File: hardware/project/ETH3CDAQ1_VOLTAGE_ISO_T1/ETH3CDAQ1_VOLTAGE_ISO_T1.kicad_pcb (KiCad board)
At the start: 4 copper layers, 80 x 30 mm, 80 parts, among them J101 GMSTB2,5/2-GF-7,62, J102 Conn_02x10_Odd_Even, U101 DG211, U102 DG419xY, U103 LT3032, U104 OPA140, U105 ISO124, U106 ADuM5410, U107 DCP020515DU, U108 OPA237_SOT23, U109 LT3032-15, U110 74LVC1GU04DRL, U111 74LVC1GU04DRL, U112 74LVC1GU04DRL, U113 24LC08B-E/MS, U114 TXB0104PW, U115 PCA9557PW

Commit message: Voltage module done.
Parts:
- added R25: 10k, Resistor_SMD:R_0603_1608Metric_Pad0.98x0.95mm_HandSolder, B.Cu at (139.8, 54.0)
- added R26: 0, Resistor_SMD:R_0603_1608Metric_Pad0.98x0.95mm_HandSolder, B.Cu at (133.9, 58.5)
- C23: renamed from C115; moved to B.Cu
- U11: renamed from U111; moved to B.Cu
- U12: renamed from U112; moved to F.Cu
- moved C21 4.44 mm to (135.1, 63.9), turned to 180 degrees
- moved C20 3.81 mm to (135.6, 70.1), turned to 180 degrees
- moved C10 3.23 mm to (112.9, 61.1)
- moved R16 3.02 mm to (112.9, 63.5), turned to 0 degrees
- moved U10 2.44 mm to (133.6, 58.2)
- moved U11 2.44 mm to (133.6, 55.9)
- moved U12 2.44 mm to (133.6, 55.9)
- moved C11 2.37 mm to (112.9, 68.6), turned to 0 degrees
- moved R15 2.30 mm to (112.0, 66.0)
- moved R22 2.03 mm to (138.8, 47.0)
- moved R23 1.65 mm to (140.6, 47.0)
- moved SYM1 1.61 mm to (103.8, 56.9)
- moved C6 1.53 mm to (113.8, 57.5)
- moved C7 1.53 mm to (113.8, 49.0)
- moved C8 1.53 mm to (111.3, 49.0)
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- renumbered C101 to C1, C127 to C10, C128 to C11, C106 to C12, C107 to C13, C129 to C14, C130 to C15, C108 to C16, C109 to C17, C110 to C18, C111 to C19, C102 to C2, C112 to C20, C113 to C21, C114 to C22, C116 to C24, C117 to C25, C118 to C26, C119 to C27, C120 to C28, C121 to C29, C103 to C3, C122 to C30, C104 to C4, C105 to C5, C123 to C6, C124 to C7, C125 to C8, C126 to C9, E101 to E1, FB101 to FB1, FB102 to FB2, FB103 to FB3, H101 to H1, H102 to H2, J101 to J1, J102 to J2, L101 to L1, R101 to R1, R110 to R10, R111 to R11, R112 to R12, R113 to R13, R114 to R14, R115 to R15, R116 to R16, R117 to R17, R118 to R18, R119 to R19, R102 to R2, R120 to R20, R121 to R21, R122 to R22, R123 to R23, R124 to R24, R103 to R3, R104 to R4, R105 to R5, R106 to R6, R107 to R7, R108 to R8, R109 to R9, RV101 to RV1, SYM101 to SYM1, U101 to U1, U110 to U10, U113 to U13, U114 to U14, U115 to U15, U102 to U2, U103 to U3, U104 to U4, U105 to U5, U106 to U6, U107 to U7, U108 to U8, U109 to U9
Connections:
- U14 pad 2: Net-(U114-Pad2) -> /IO5
- U14 pad 3: Net-(U114-Pad3) -> /IO4
- U14 pad 4: Net-(U114-Pad4) -> /IO3
- U14 pad 5: Net-(U114-Pad5) -> /IO2
- U14 pad 8: (no net) -> Net-(R25-Pad2)
- U15 pad 10: Net-(U114-Pad3) -> /IO3
- U15 pad 11: Net-(U114-Pad4) -> /IO4
- U15 pad 12: Net-(U114-Pad5) -> /IO5
- U15 pad 9: Net-(U114-Pad2) -> /IO2
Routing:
- net AGNDF: track 0.00 -> 96.2 mm, vias 0 -> 27
- net (no net): track 0.00 -> 71.1 mm
- net +5VF: track 0.00 -> 48.8 mm, vias 0 -> 6
- net -15VF: track 0.00 -> 39.8 mm, vias 0 -> 10
- net +15VF: track 0.00 -> 28.1 mm, vias 0 -> 7
- net /SCL: track 0.00 -> 25.2 mm, vias 0 -> 1
- net Net-(R15-Pad1): track 0.00 -> 22.7 mm, vias 0 -> 2
- net /AOUT: track 0.00 -> 22.7 mm
- net /G1: track 0.00 -> 21.8 mm
- net /G10: track 0.00 -> 20.0 mm, vias 0 -> 2
- net Net-(U1-Pad11): track 0.00 -> 18.6 mm
- net Net-(R20-Pad2): track 0.00 -> 18.4 mm, vias 0 -> 1
- net /A0: track 0.00 -> 18.0 mm, vias 0 -> 1
- net /SDA: track 0.00 -> 17.9 mm, vias 0 -> 1
- net Net-(C1-Pad1): track 0.00 -> 16.4 mm
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- added copper zone on B.Cu, net +15V
- added copper zone on F.Cu, net +15V
- added copper zone on In2.Cu, net +15V
- added copper zone on B.Cu, net +15VF
- added copper zone on F.Cu, net +15VF
- added copper zone on In2.Cu, net +15VF
- added copper zone on In2.Cu, net +18V
- added copper zone on In2.Cu, net +3V3
- added copper zone on B.Cu, net +5V
- added copper zone on F.Cu, net +5V
- added copper zone on In2.Cu, net +5V
- added copper zone on B.Cu, net -15V
- added copper zone on F.Cu, net -15V
- added copper zone on In2.Cu, net -15V
- added copper zone on B.Cu, net -15VF
- added copper zone on F.Cu, net -15VF
- added copper zone on In2.Cu, net -15VF
- added copper zone on In2.Cu, net -18V
- added copper zone on F.Cu, net AGNDF
- added copper zone on In1.Cu, net AGNDF
- added copper zone on B.Cu, net GND
- added copper zone on F.Cu, net GND
- added copper zone on In1.Cu, net GND
- added copper zone on B.Cu, net VCC
- added copper zone on F.Cu, net VCC
- added copper zone on In2.Cu, net VCC
- added copper zone on B.Cu, net VDD
- added copper zone on F.Cu, net VDD
- added copper zone on In2.Cu, net VDD
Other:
- outline, holes or cut-outs redrawn
- net class Default: clearance 0.2 -> 0.127; trace_width 0.25 -> 0.127; via_dia 0.8 -> 0.5; via_drill 0.4 -> 0.2
- rule trace_clearance: 0.2 -> 0.127
- rule trace_min: 0.2 -> 0.12
- rule via_min_drill: 0.3 -> 0.2
- board text added: "1"
- board text added: "2"
- board text added: "3"
- board text added: "4"
- board text added: "ONLY PLASTIC SPACER"

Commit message: Modifications in PCBs.
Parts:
- moved C30 0.65 mm to (140.6, 50.8)
- moved R24 0.65 mm to (138.8, 50.8)

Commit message: PCB design
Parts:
- added C31: 10u, Capacitor_SMD:C_0603_1608Metric_Pad1.08x0.95mm_HandSolder, B.Cu at (134.0, 48.5)
- added C32: 100n, Capacitor_SMD:C_0603_1608Metric_Pad1.08x0.95mm_HandSolder, B.Cu at (134.0, 46.1)
- C14, C15: value 100n -> 10u
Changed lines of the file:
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@@
-(kicad_pcb (version 20171130) (host pcbnew "(5.1.8)-1")
+(kicad_pcb (version 20171130) (host pcbnew 5.1.8)
   (general
     (thickness 1.6)
@@
     (tracks 778)
     (zones 0)
-    (modules 82)
+    (modules 84)
     (nets 65)
   )
@@
   )
   (setup
-    (last_trace_width 0.381)
+    (last_trace_width 0.127)
     (user_trace_width 0.254)
     (user_trace_width 0.381)
@@
     (add_net "Net-(C5-Pad2)")
     (add_net "Net-(E1-Pad1)")
+    (add_net "Net-(J2-Pad17)")
+    (add_net "Net-(J2-Pad5)")
+    (add_net "Net-(J2-Pad6)")
     (add_net "Net-(L1-Pad2)")
     (add_net "Net-(R1-Pad2)")
@@
     (add_net "Net-(U1-Pad11)")
     (add_net "Net-(U1-Pad6)")
+    (add_net "Net-(U10-Pad1)")
+    (add_net "Net-(U11-Pad1)")
     (add_net "Net-(U11-Pad2)")
+    (add_net "Net-(U12-Pad1)")
     (add_net "Net-(U12-Pad2)")
+    (add_net "Net-(U14-Pad6)")
+    (add_net "Net-(U14-Pad9)")
+    (add_net "Net-(U15-Pad13)")
+    (add_net "Net-(U15-Pad14)")
+    (add_net "Net-(U15-Pad6)")
     (add_net "Net-(U2-Pad1)")
+    (add_net "Net-(U3-Pad13)")
+    (add_net "Net-(U4-Pad1)")
+    (add_net "Net-(U4-Pad5)")
+    (add_net "Net-(U4-Pad8)")
+    (add_net "Net-(U6-Pad17)")
+    (add_net "Net-(U6-Pad7)")
+    (add_net "Net-(U6-Pad8)")
+    (add_net "Net-(U9-Pad13)")
+    (add_net "Net-(U9-Pad2)")
+    (add_net "Net-(U9-Pad8)")
     (add_net VCC)
     (add_net VDD)
   )
+  (module Capacitor_SMD:C_0603_1608Metric_Pad1.08x0.95mm_HandSolder (layer B.Cu)
+    (at 133.985 46.101 180)
+    (descr "Capacitor SMD 0603 (1608 Metric), square (rectangular) end terminal, IPC_7351 nominal with elongated pad for handsoldering. (Body size source: IPC-SM-782 page 76, https://www.pcb-3d.com/wordpress/wp-content/uploads/ipc-sm-782a_amendment_1_and_2.pdf), generated with kicad-footprint-generator")
+    (tags "capacitor handsolder")
+    (attr smd)
+    (fp_text reference C32 (at 0 1.113) (layer B.SilkS)
+      (effects (font (size 0.6 0.6) (thickness 0.12)) (justify mirror))
+    )
+    (fp_text value 100n (at 0 -1.43) (layer B.Fab)
+      (effects (font (size 1 1) (thickness 0.15)) (justify mirror))
+    )
+    (fp_line (start 1.65 -0.73) (end -1.65 -0.73) (layer B.CrtYd) (width 0.05))
+    (fp_line (start 1.65 0.73) (end 1.65 -0.73) (layer B.CrtYd) (width 0.05))
+    (fp_line (start -1.65 0.73) (end 1.65 0.73) (layer B.CrtYd) (width 0.05))
+    (fp_line (start -1.65 -0.73) (end -1.65 0.73) (layer B.CrtYd) (width 0.05))
+    (fp_line (start -0.146267 -0.51) (end 0.146267 -0.51) (layer B.SilkS) (width 0.12))
+    (fp_line (start -0.146267 0.51) (end 0.146267 0.51) (layer B.SilkS) (width 0.12))
+    (fp_line (start 0.8 -0.4) (end -0.8 -0.4) (layer B.Fab) (width 0.1))
+    (fp_line (start 0.8 0.4) (end 0.8 -0.4) (layer B.Fab) (width 0.1))
+    (fp_line (start -0.8 0.4) (end 0.8 0.4) (layer B.Fab) (width 0.1))
+    (fp_line (start -0.8 -0.4) (end -0.8 0.4) (layer B.Fab) (width 0.1))
+    (fp_text user %R (at 0 0) (layer B.Fab)
+      (effects (font (size 0.4 0.4) (thickness 0.06)) (justify mirror))
+    )
+    (pad 2 smd roundrect (at 0.8625 0 180) (size 1.075 0.95) (layers B.Cu B.Paste B.Mask) (roundrect_rratio 0.25)
+      (net 6 GND))
+    (pad 1 smd roundrect (at -0.8625 0 180) (size 1.075 0.95) (layers B.Cu B.Paste B.Mask) (roundrect_rratio 0.25)
+      (net 7 +5V))
+    (model ${KISYS3DMOD}/Capacitor_SMD.3dshapes/C_0603_1608Metric.wrl
+      (at (xyz 0 0 0))
+      (scale (xyz 1 1 1))
+      (rotate (xyz 0 0 0))
+    )
+  )
+  (module Capacitor_SMD:C_0603_1608Metric_Pad1.08x0.95mm_HandSolder (layer B.Cu)
+    (at 133.985 48.514 180)
+    (descr "Capacitor SMD 0603 (1608 Metric), square (rectangular) end terminal, IPC_7351 nominal with elongated pad for handsoldering. (Body size source: IPC-SM-782 page 76, https://www.pcb-3d.com/wordpress/wp-content/uploads/ipc-sm-782a_amendment_1_and_2.pdf), generated with kicad-footprint-generator")
+    (tags "capacitor handsolder")
+    (attr smd)
+    (fp_text reference C31 (at 0 1.143) (layer B.SilkS)
+      (effects (font (size 0.6 0.6) (thickness 0.12)) (justify mirror))
+    )
+    (fp_text value 10u (at 0 -1.43) (layer B.Fab)
+      (effects (font (size 1 1) (thickness 0.15)) (justify mirror))
+    )
+    (fp_line (start 1.65 -0.73) (end -1.65 -0.73) (layer B.CrtYd) (width 0.05))
+    (fp_line (start 1.65 0.73) (end 1.65 -0.73) (layer B.CrtYd) (width 0.05))
+    (fp_line (start -1.65 0.73) (end 1.65 0.73) (layer B.CrtYd) (width 0.05))
+    (fp_line (start -1.65 -0.73) (end -1.65 0.73) (layer B.CrtYd) (width 0.05))
+    (fp_line (start -0.146267 -0.51) (end 0.146267 -0.51) (layer B.SilkS) (width 0.12))
+    (fp_line (start -0.146267 0.51) (end 0.146267 0.51) (layer B.SilkS) (width 0.12))
+    (fp_line (start 0.8 -0.4) (end -0.8 -0.4) (layer B.Fab) (width 0.1))
+    (fp_line (start 0.8 0.4) (end 0.8 -0.4) (layer B.Fab) (width 0.1))
+    (fp_line (start -0.8 0.4) (end 0.8 0.4) (layer B.Fab) (width 0.1))
+    (fp_line (start -0.8 -0.4) (end -0.8 0.4) (layer B.Fab) (width 0.1))
+    (fp_text user %R (at 0 0) (layer B.Fab)
+      (effects (font (size 0.4 0.4) (thickness 0.06)) (justify mirror))
+    )
+    (pad 2 smd roundrect (at 0.8625 0 180) (size 1.075 0.95) (layers B.Cu B.Paste B.Mask) (roundrect_rratio 0.25)
+      (net 6 GND))
+    (pad 1 smd roundrect (at -0.8625 0 180) (size 1.075 0.95) (layers B.Cu B.Paste B.Mask) (roundrect_rratio 0.25)
+      (net 7 +5V))
+    (model ${KISYS3DMOD}/Capacitor_SMD.3dshapes/C_0603_1608Metric.wrl
+      (at (xyz 0 0 0))
+      (scale (xyz 1 1 1))
+      (rotate (xyz 0 0 0))
+    )
+  )
   (module ETH3CDAQ1:NLV32 (layer B.Cu)
     (at 83.947 52.959)
@@
       (effects (font (size 0.6 0.6) (thickness 0.12)) (justify mirror))
     )
-    (fp_text value 100n (at 0 -1.43) (layer B.Fab)
+    (fp_text value 10u (at 0 -1.43) (layer B.Fab)
       (effects (font (size 0.6 0.6) (thickness 0.12)) (justify mirror))
     )
@@
       (effects (font (size 0.6 0.6) (thickness 0.12)) (justify mirror))
     )
-    (fp_text value 100n (at 0 -1.43) (layer B.Fab)
+    (fp_text value 10u (at 0 -1.43) (layer B.Fab)
       (effects (font (size 0.6 0.6) (thickness 0.12)) (justify mirror))
     )
@@
     (polygon
       (pts
-        (xy 136.144 44.958) (xy 134.112 44.958) (xy 134.112 42.291) (xy 136.144 42.291)
+        (xy 136.398 49.657) (xy 134.112 49.657) (xy 134.112 42.291) (xy 136.398 42.291)
       )
     )

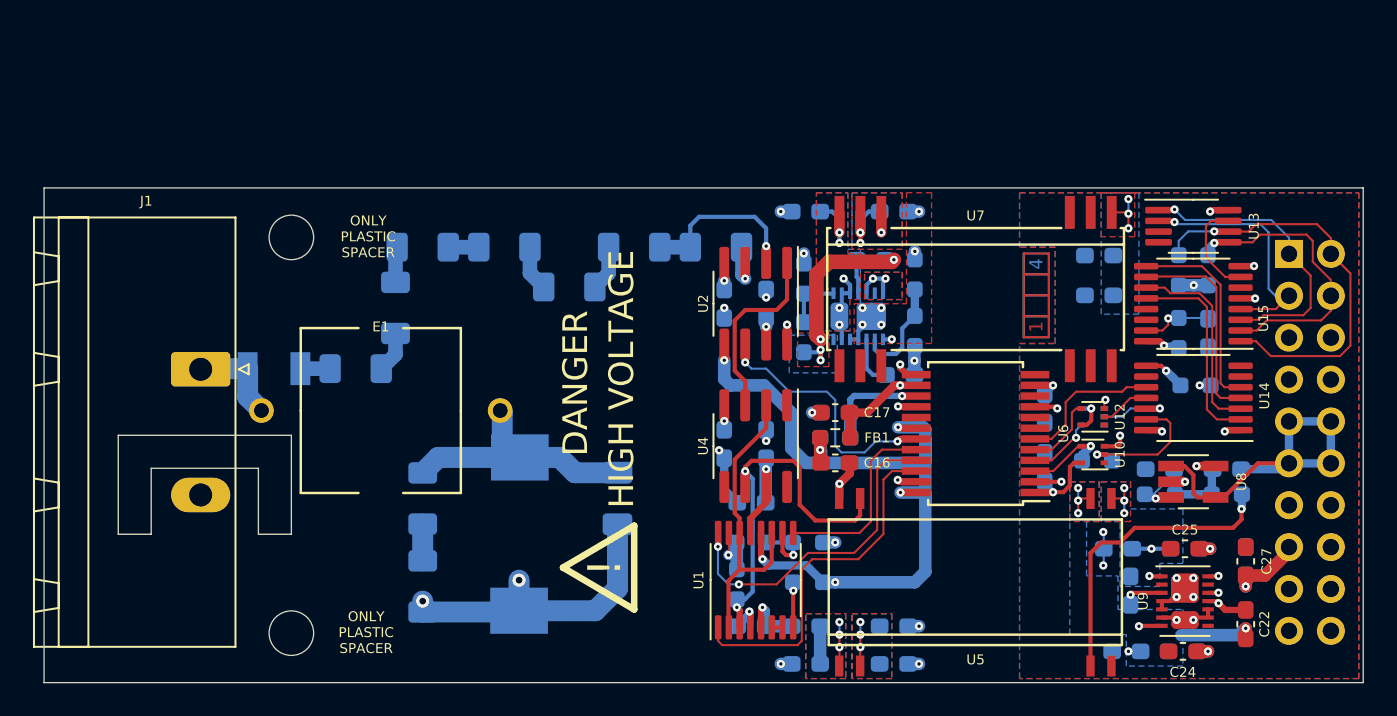
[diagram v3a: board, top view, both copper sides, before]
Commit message: Modification in PCBs. Created BOM files.
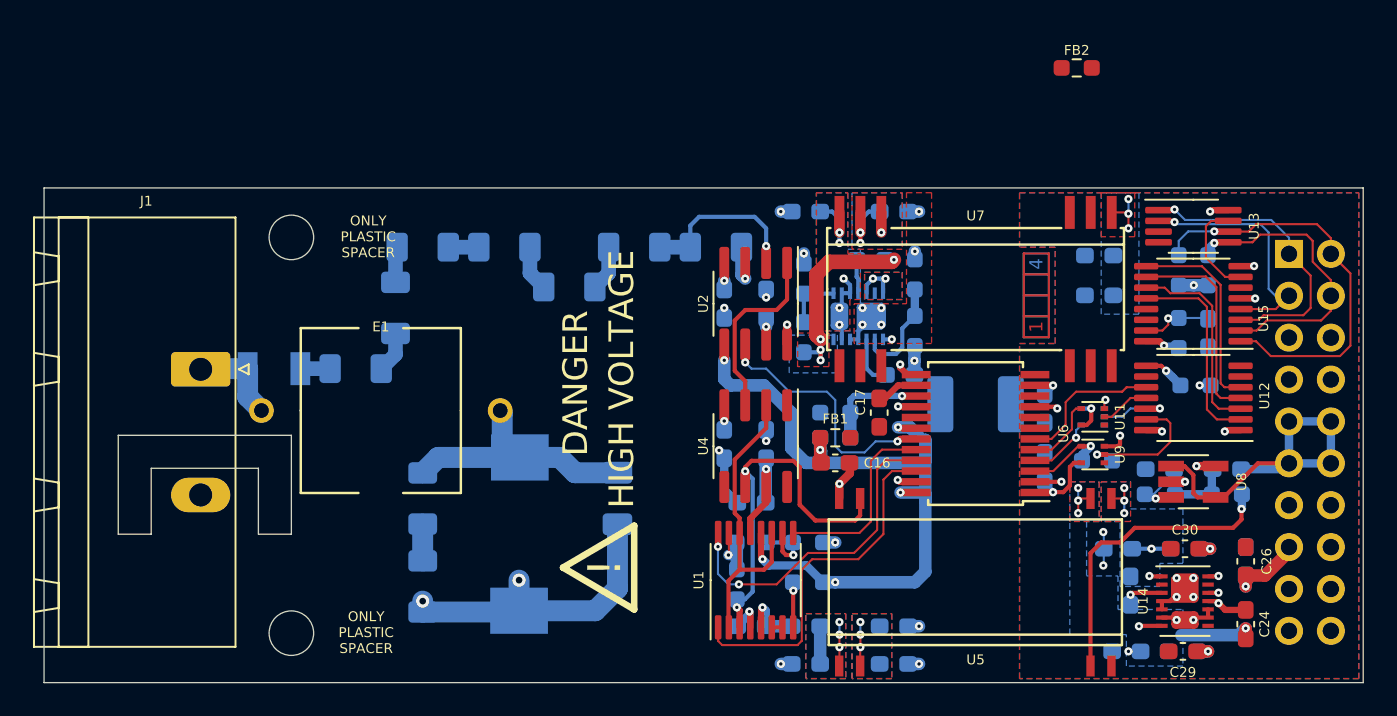
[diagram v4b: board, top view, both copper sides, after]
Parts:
- added C18: C, Capacitor_SMD:C_1812_4532Metric_Pad1.57x3.40mm_HandSolder, B.Cu at (126.5, 55.1)
- added FB2: FB, Resistor_SMD:R_0603_1608Metric_Pad0.98x0.95mm_HandSolder, F.Cu at (132.6, 34.7)
- moved C17 2.67 mm to (120.7, 55.6), turned to 270 degrees
- renumbered C18 to C19, C19 to C20, C20 to C21, C21 to C22, C26 to C23, C22 to C24, C23 to C25, C27 to C26, C28 to C27, C29 to C28, C24 to C29, C25 to C30, C30 to C33, FB2 to FB3, FB3 to FB4, R6 to R1, R7 to R2, R26 to R22, R25 to R23, R22 to R24, R24 to R25, R23 to R26, R8 to R3, R9 to R4, R1 to R5, R2 to R6, R3 to R7, R4 to R8, R5 to R9, U11 to U10, U12 to U11, U14 to U12, U9 to U14, U10 to U9
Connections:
- C17 pad 2: AGNDF -> Net-(C17-Pad2)
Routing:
- net Net-(C17-Pad1): track 6.28 -> 2.57 mm, vias 1 -> 0
- net AGNDF: track 96.2 -> 95.2 mm, vias 27 -> 26
- net +5VF: track 48.8 -> 47.8 mm

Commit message: PCB modifications
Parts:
- moved FB2 5.03 mm to (127.6, 34.3)

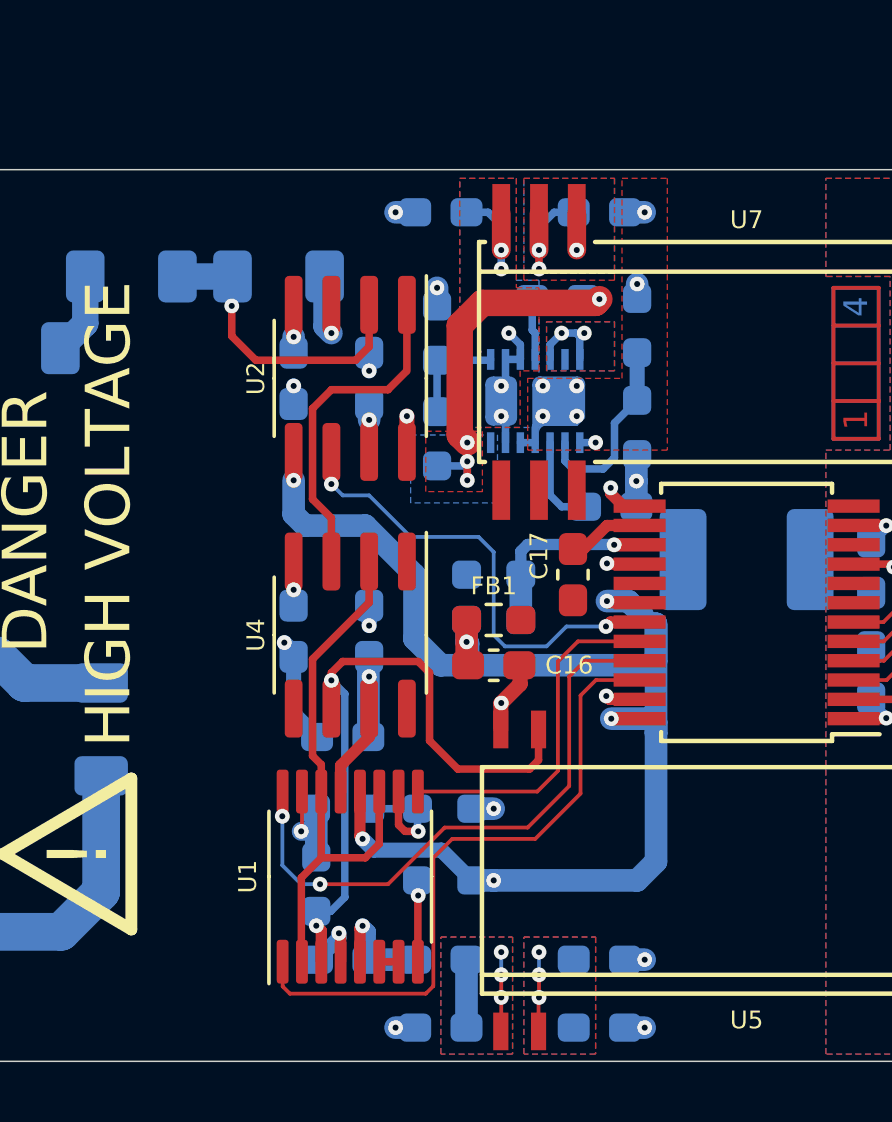
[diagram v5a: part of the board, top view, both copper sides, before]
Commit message: Added SDRAM to the linker file.
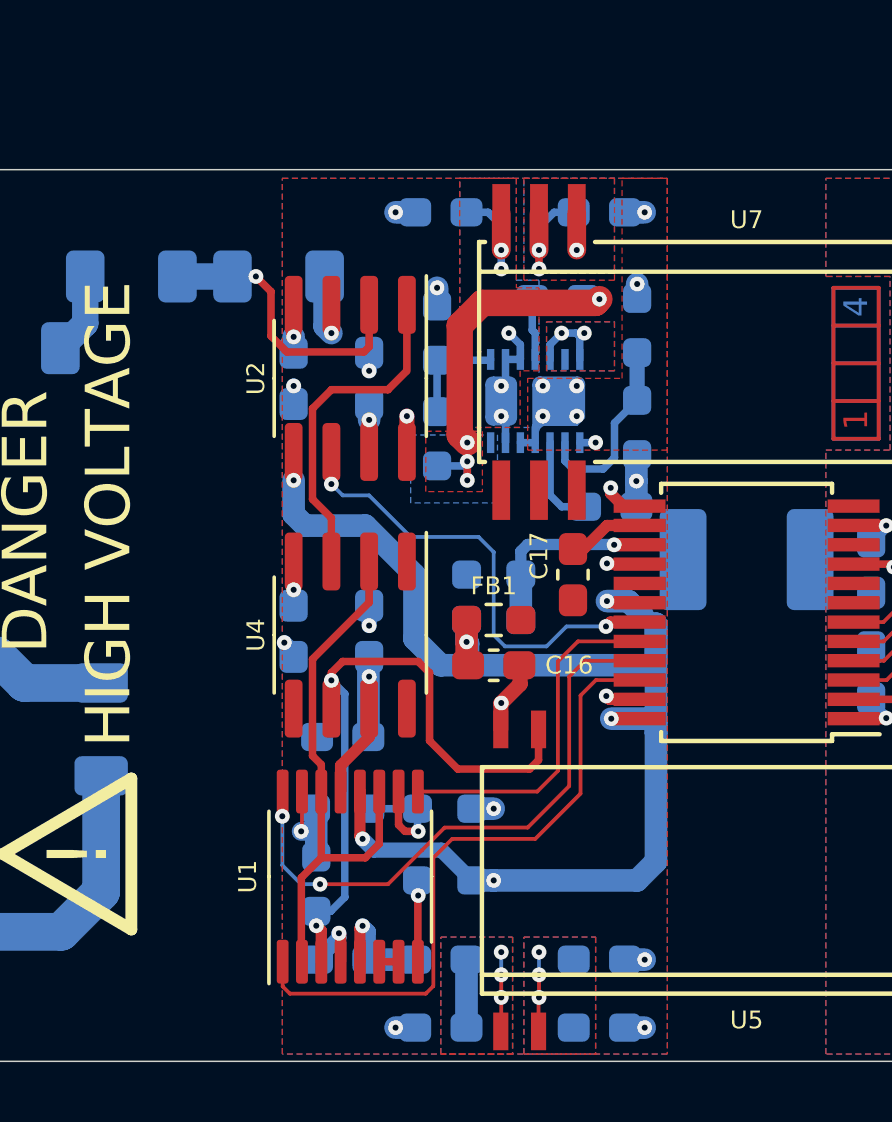
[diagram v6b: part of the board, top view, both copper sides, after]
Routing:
- net AGNDF: track 95.3 -> 92.3 mm
- net Net-(R12-Pad1): track 10.4 -> 9.86 mm
- added copper zone on B.Cu, net AGNDF
